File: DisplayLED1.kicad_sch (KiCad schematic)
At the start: 72 parts

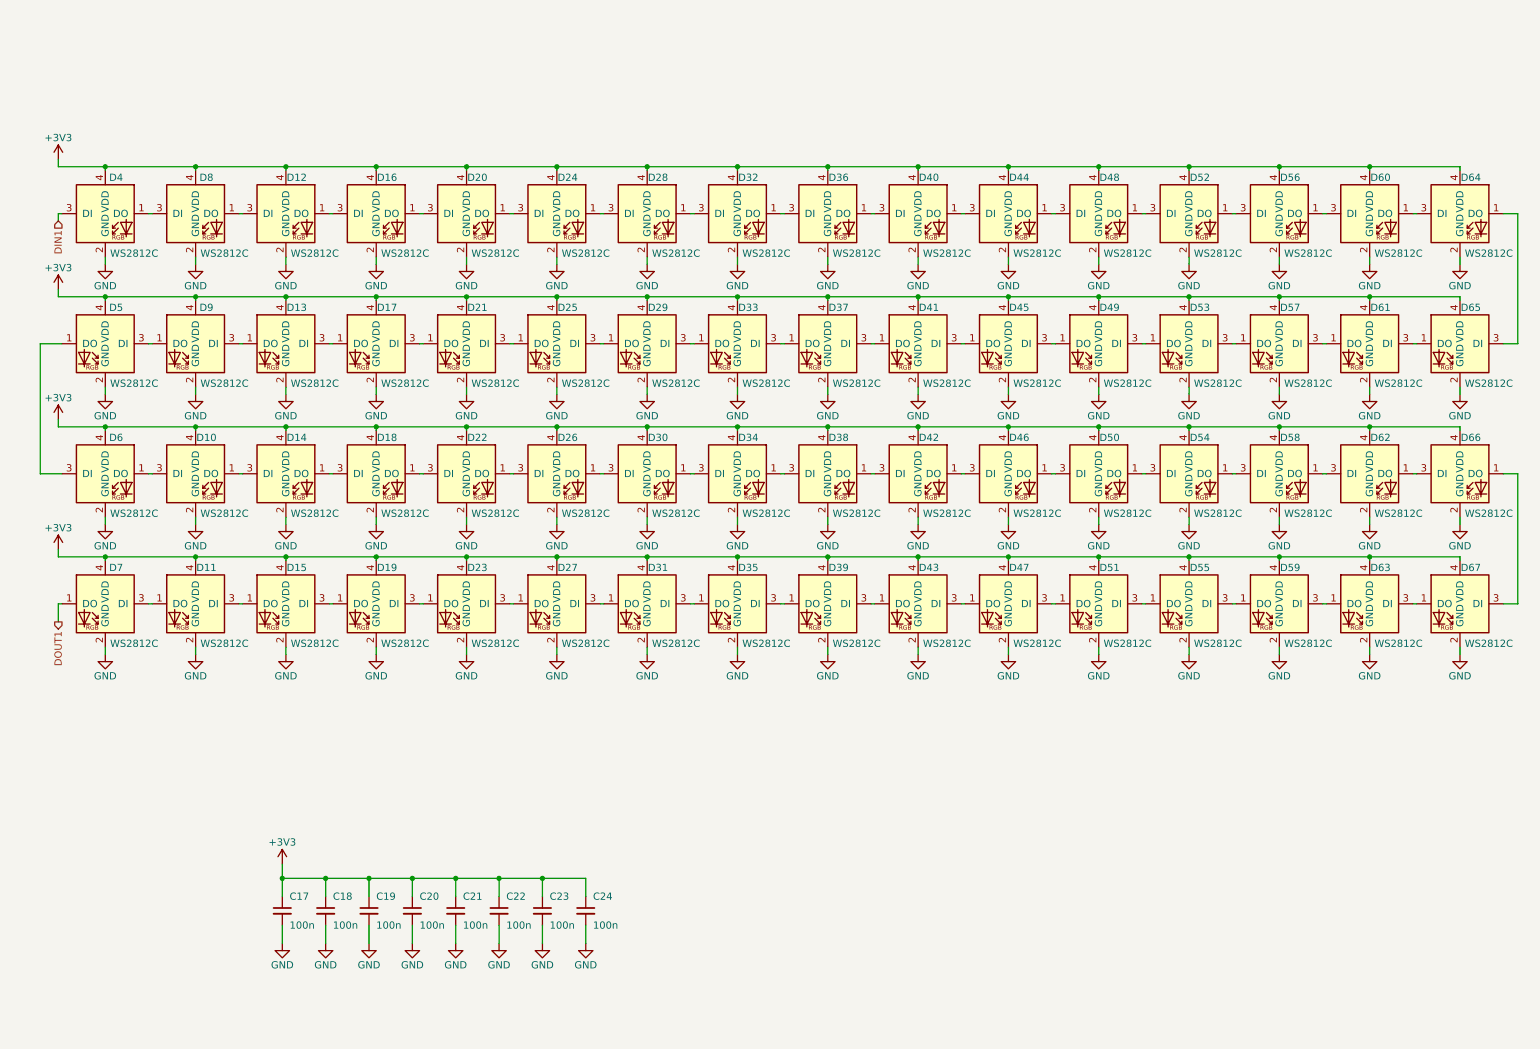
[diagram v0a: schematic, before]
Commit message: Schematic finished, routing PCB started.
Signed-off-by: Ion Bold <bold.ion86@gmail.com>
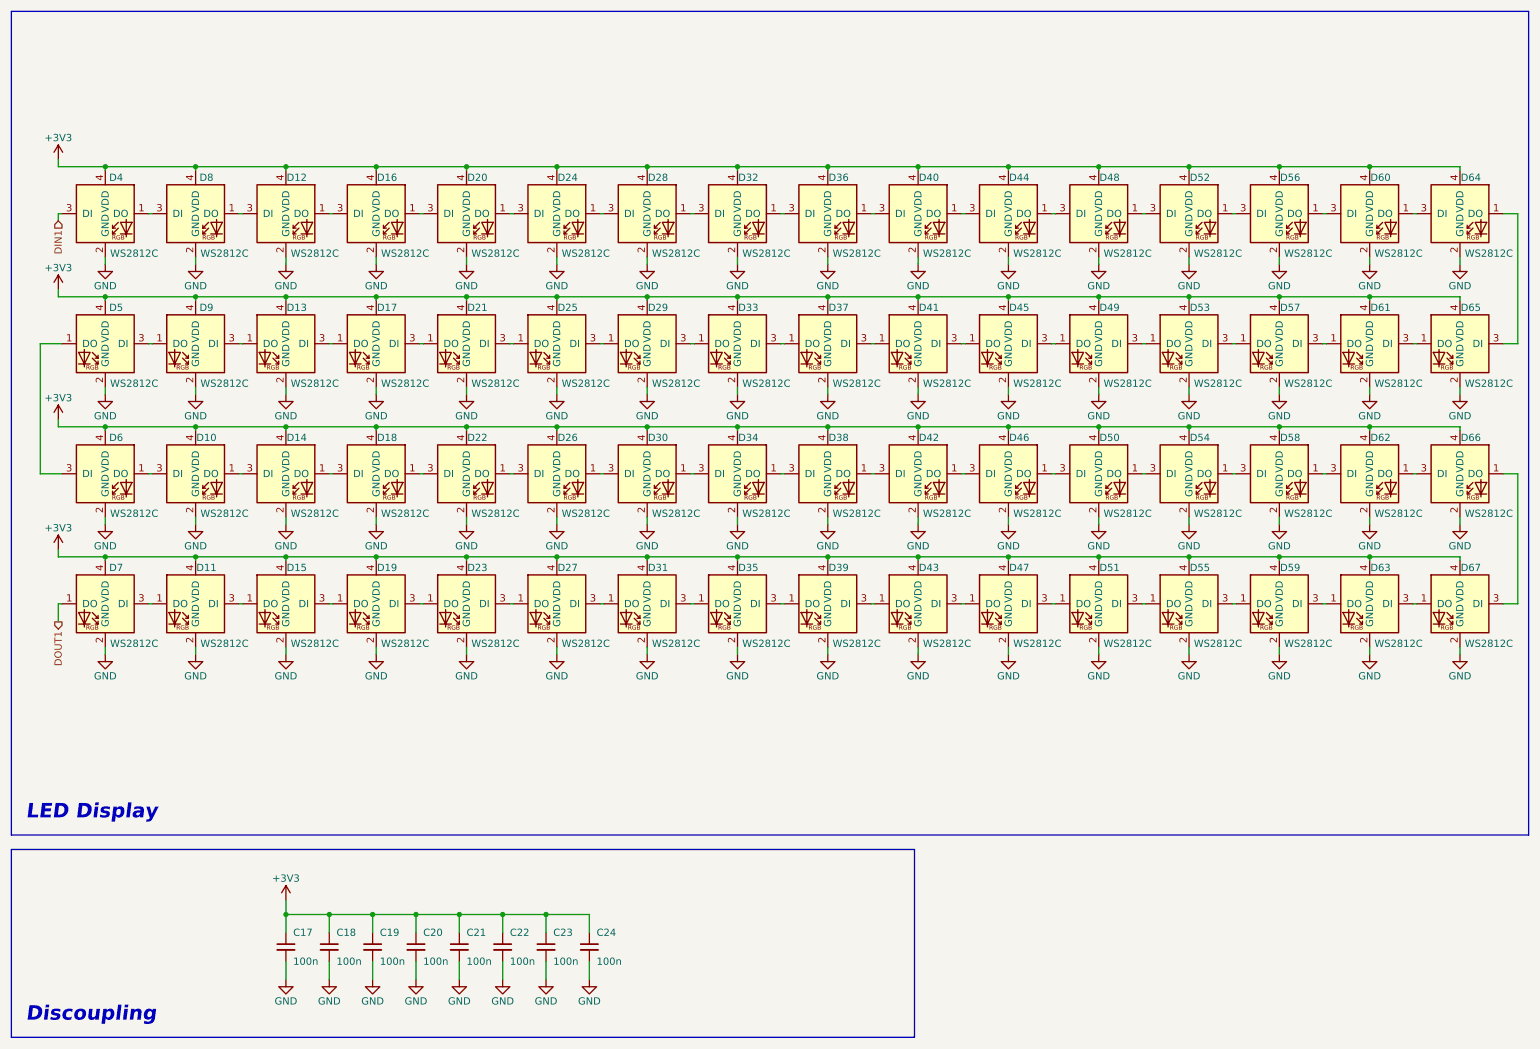
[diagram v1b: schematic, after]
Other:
- note added: "Discoupling"
- note added: "LED Display"
- moved on the sheet: C17, C18, C19, C20, C21, C22, C23, C24
